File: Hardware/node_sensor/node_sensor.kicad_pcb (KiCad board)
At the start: 2 copper layers, 8 parts, among them U3 E32-433, U4 DevKitSTM32, U5 BMP-388, U6 SHT30

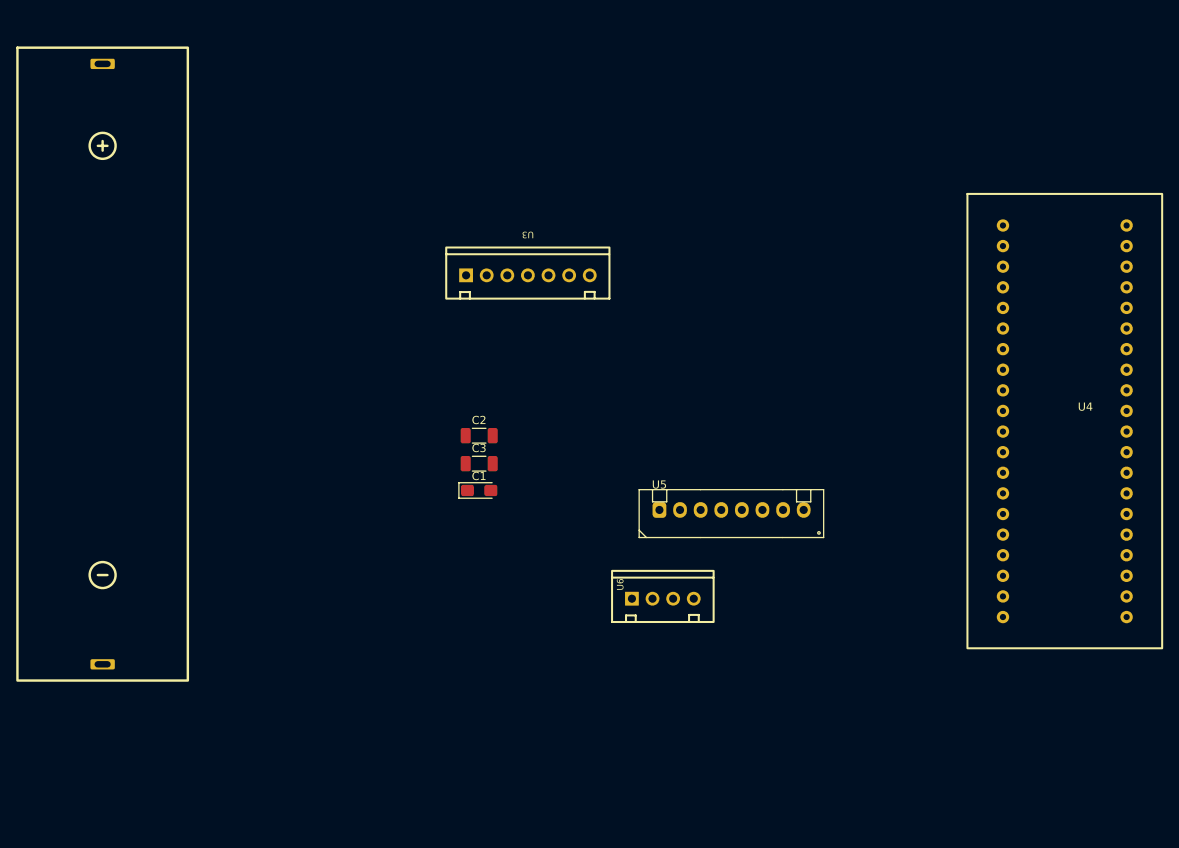
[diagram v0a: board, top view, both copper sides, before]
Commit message: completed node_sensor v1.1
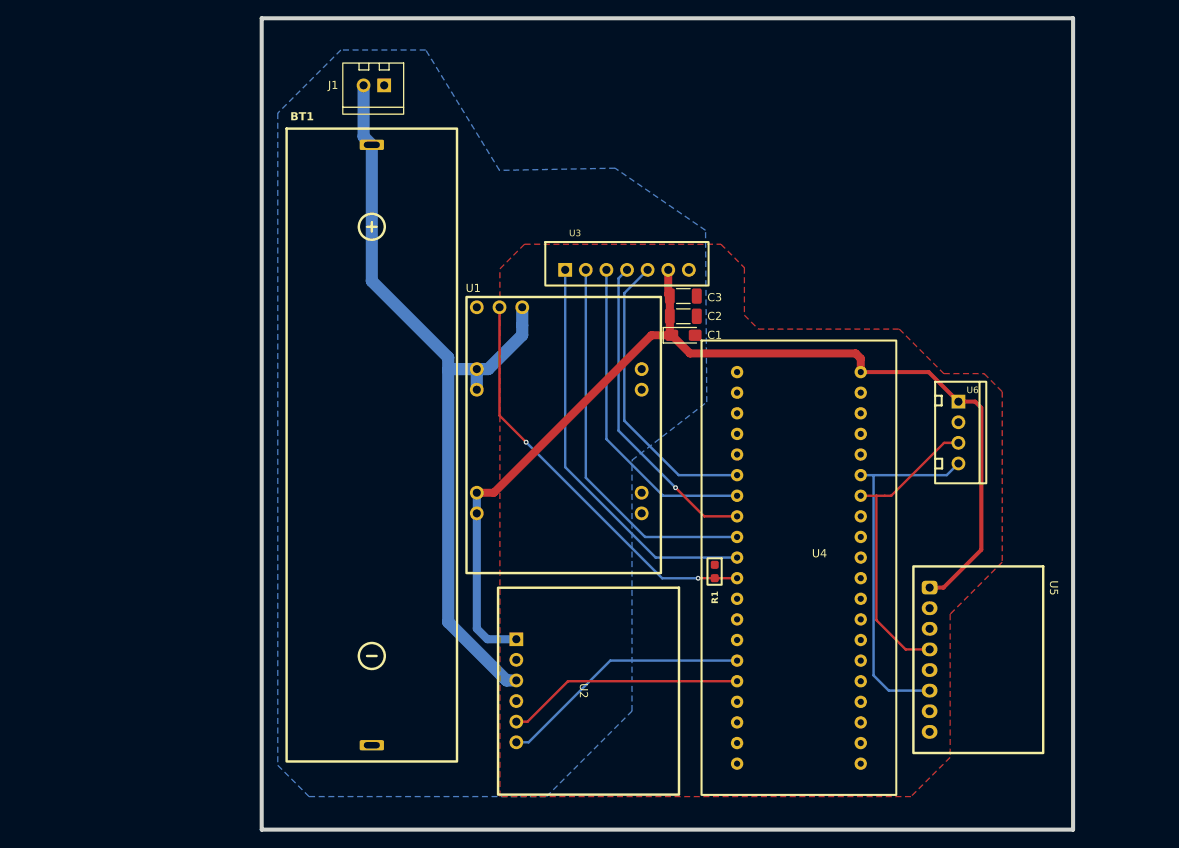
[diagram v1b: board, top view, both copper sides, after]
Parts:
- added J1: Solar_Pannel, iot_footprint:XH 2.54 2Pin Female, F.Cu at (121.3, 43.3)
- added R1: 10k, iot_footprint:R0603, F.Cu at (165.8, 103.2)
- added U1: TPS63020, course_kicad_ecp_footprint:TPS63020-module, F.Cu at (136.5, 70.6)
- added U2: INA219, course_kicad_ecp_footprint:INA219, F.Cu at (141.4, 117.9)
- U5: footprint iot_footprint:XH_8P_2.54mm_Vertical -> course_kicad_ecp_footprint:BMP388-module
- moved U6 41.8 mm to (195.9, 86.1), turned to 0 degrees
- moved U4 37.4 mm to (176.2, 101.5)
- moved U5 34.6 mm to (192.3, 105.2), turned to -90 degrees
- moved BT1 34.6 mm to (123.6, 87.6)
- moved C3 32.6 mm to (162.0, 69.2)
- moved C1 31.6 mm to (162.0, 74.1)
- moved C2 29.2 mm to (162.0, 71.7)
- moved U3 12.3 mm to (155.0, 65.4), turned to 0 degrees
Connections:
- U6 pad 3: (no net) -> /PB6
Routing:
- net +3.3V: track 0.00 -> 131.1 mm
- net /Pin+: track 0.00 -> 98.7 mm
- net /PA6: track 0.00 -> 50.9 mm, vias 0 -> 2
- net /PA5: track 0.00 -> 50.1 mm
- net /PA4: track 0.00 -> 47.3 mm
- net /PB7: track 0.00 -> 45.0 mm
- net /PA2: track 0.00 -> 39.9 mm
- net /PA3: track 0.00 -> 39.2 mm, vias 0 -> 1
- net /PB6: track 0.00 -> 38.1 mm
- net /PA1: track 0.00 -> 36.5 mm
- net /PB10: track 0.00 -> 31.4 mm
- net /PB11: track 0.00 -> 29.3 mm
- added copper zone on B.Cu, net /Pin-
- added copper zone on F.Cu, net GND
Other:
- board outline added: 100 x 100 mm

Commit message: completed v1 node sensor
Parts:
- added ?: , , F.Cu at (207.5, 37.5)
- added ?: , , F.Cu at (112.5, 37.5)
- added ?: , , F.Cu at (112.5, 132.5)
- added ?: , , F.Cu at (207.5, 132.5)
- added U7: BMS-1s, MY_FOOTPRINTS:BMS-1s-18560, B.Cu at (128.4, 66.6)
- BT1: footprint course_kicad_ecp_footprint:Battery-18560-1s -> Battery:BatteryHolder_MPD_BH-18650-PC
- C2, C3: footprint Inductor_SMD:L_1206_3216Metric_Pad1.22x1.90mm_HandSolder -> MY_FOOTPRINTS:C_0805
- J1: footprint iot_footprint:XH 2.54 2Pin Female -> MY_FOOTPRINTS:Conn_XH-P2.54mm-2P
- R1: footprint iot_footprint:R0603 -> MY_FOOTPRINTS:R0603
- U1: footprint course_kicad_ecp_footprint:TPS63020-module -> MY_FOOTPRINTS:TPS63020-module
- U2: footprint course_kicad_ecp_footprint:INA219 -> MY_FOOTPRINTS:INA219
- U3: footprint iot_footprint:Conn_XH-P2.54mm-7P -> Connector_PinSocket_2.54mm:PinSocket_1x07_P2.54mm_Vertical
- U4: footprint iot_footprint:DevKitSTM32 -> MY_FOOTPRINTS:DevKitSTM32
- U5: footprint course_kicad_ecp_footprint:BMP388-module -> MY_FOOTPRINTS:BMP388-module
- U6: footprint iot_footprint:Conn_XH-P2.54mm-4P -> Connector_JST:JST_XH_B4B-XH-A_1x04_P2.50mm_Vertical
- moved BT1 36.7 mm to (123.2, 51.0), turned to -90 degrees
- moved U3 7.63 mm to (147.4, 66.0), turned to 90 degrees
- moved U6 3.79 mm to (195.9, 82.3), turned to -90 degrees
- moved J1 2.72 mm to (123.9, 44.0), turned to 90 degrees
- moved R1 2.65 mm to (165.5, 105.8), turned to 90 degrees
- moved C1 1.36 mm to (162.0, 72.7)
- moved C2 1.28 mm to (161.3, 70.6)
- moved U4 1.03 mm to (176.2, 102.5)
- moved C3 0.82 mm to (161.3, 68.7)
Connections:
- J1 pad 1: /Pin- -> /Pin+
- J1 pad 2: /Pin+ -> /Pin-
- U1 pad 1: /Pin+ -> Net-(U1-EN)
- U1 pad 2: /Pin- -> GND
- U1 pad 3: /Pin+ -> Net-(U1-EN)
- U2 pad 3: /Pin+ -> /PB10
- U2 pad 4: /Pin- -> /PB11
- U2 pad 5: /PB11 -> unconnected-(U2-VIN--Pad5)
- U2 pad 6: /PB10 -> Net-(U1-EN)
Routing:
- net Net-(U1-EN): track 0.00 -> 71.8 mm
- net /Pin+: track 98.7 -> 29.5 mm
- net /PB7: track 45.0 -> 41.3 mm
- net /PB10: track 31.4 -> 27.8 mm
- net /PA1: track 36.5 -> 34.7 mm
- net /PB11: track 29.3 -> 27.8 mm
- net /PB6: track 38.1 -> 37.2 mm
- net /PA6: track 50.9 -> 51.5 mm
- net GND: vias 0 -> 6
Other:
- board text added: "LE DUC TRI NGUYEN THAI ANH"
